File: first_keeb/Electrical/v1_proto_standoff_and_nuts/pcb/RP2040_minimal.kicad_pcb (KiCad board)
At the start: 4 copper layers, 67.1 x 66.8 mm, 81 parts, among them J1 Conn_01x04_Socket, J2 Conn_01x04_Socket, P1 USB-TYPE-C-016, Q1 SN74LV1T34DBV, SW1 SKRKAHE020, SW2 SKRKAHE020, SW3 BUTT1, SW4 BUTT3, SW5 BUTT2, SW6 MS-22C01-G010, SW7 SK-3296S-01-L3, SW8 MS-22C01-G010, U1 AMS1117-2.5, U2 ME6208A44M3G, U3 PRTR5V0U2X, U4 STM32F401RCTx, U5 MCP6001-OT, U6 MCP6001-OT, Y1 16MHz

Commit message: fixes lcsc number in bom
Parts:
- U7, U8, U9: value ~ -> SLSS49E
- Y1: value 16MHz -> 8MHz
- moved C13 0.05 mm to (83.7, 85.6)
- renumbered R5 to R4, R8 to R5, SW7 to SW1, SW6 to SW2, SW1 to SW3, SW8 to SW4, SW2 to SW5, SW3 to SW6, SW4 to SW7, SW5 to SW8, U5 to U4, U4 to U5
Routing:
- net GND: vias 230 -> 251

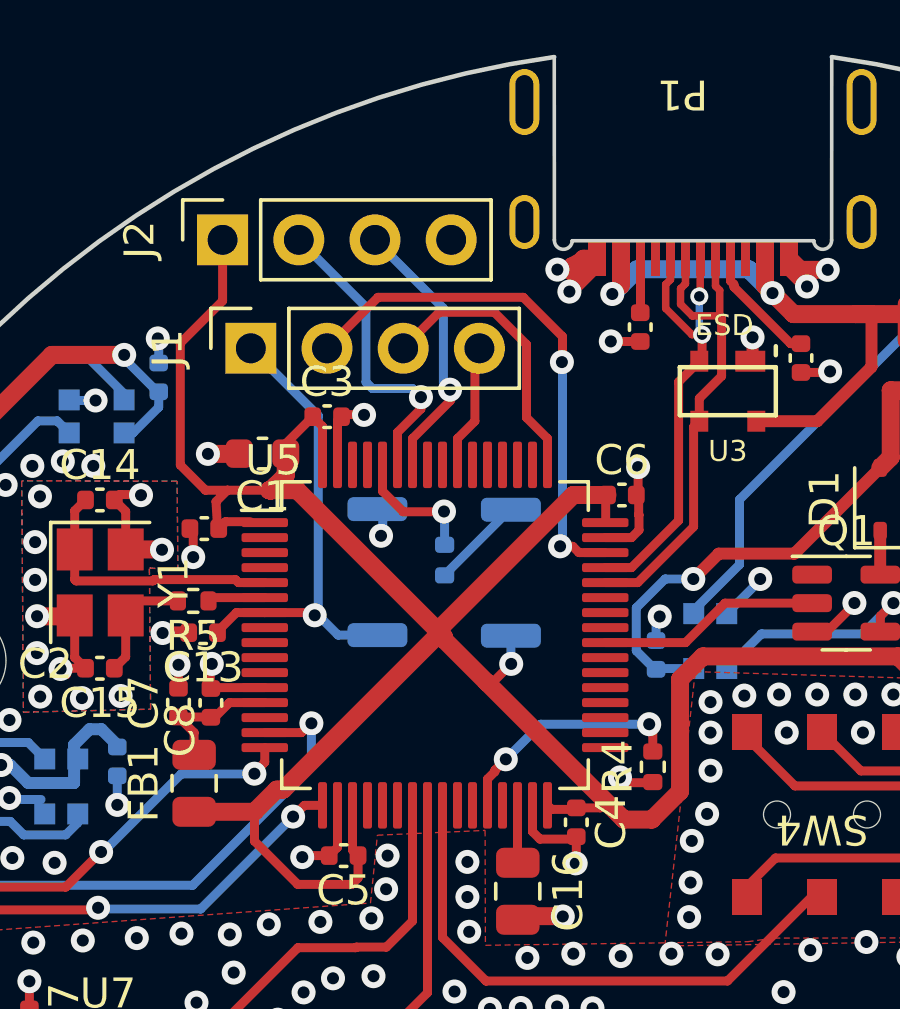
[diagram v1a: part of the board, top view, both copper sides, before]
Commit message: adds  basic part switch
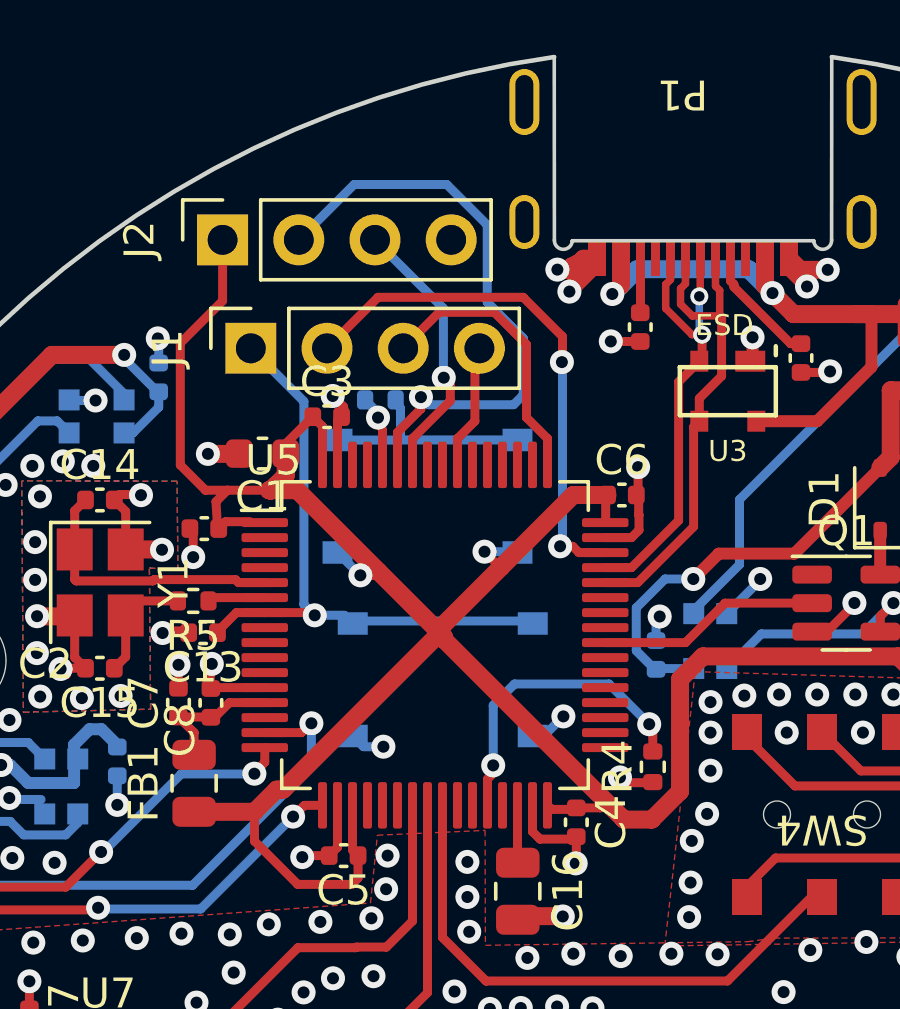
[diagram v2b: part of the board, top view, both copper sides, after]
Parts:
- SW3, SW5: value SKRKAHE020 -> TS-1187A-B-A-B; footprint Button_Switch_SMD:SW_Push_SPST_NO_Alps_SKRK -> Button_Switch_SMD:TS-1187A
- moved R3 5.75 mm to (89.6, 77.8), turned to 180 degrees
- moved SW5 4.20 mm to (91.7, 87.1), turned to 180 degrees
- moved SW3 3.77 mm to (91.2, 81.0), turned to 180 degrees
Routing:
- net USART1_RX: track 10.3 -> 20.0 mm
- net NRST: track 16.3 -> 20.7 mm
- net Net-(R3-Pad1): track 3.13 -> 7.03 mm
- net BOOT1: track 8.35 -> 10.8 mm
- net BOOT0: track 4.42 -> 2.37 mm
- net VDD: track 90.1 -> 91.6 mm, vias 1 -> 2
- net GND: track 123.2 -> 124.8 mm, vias 251 -> 252

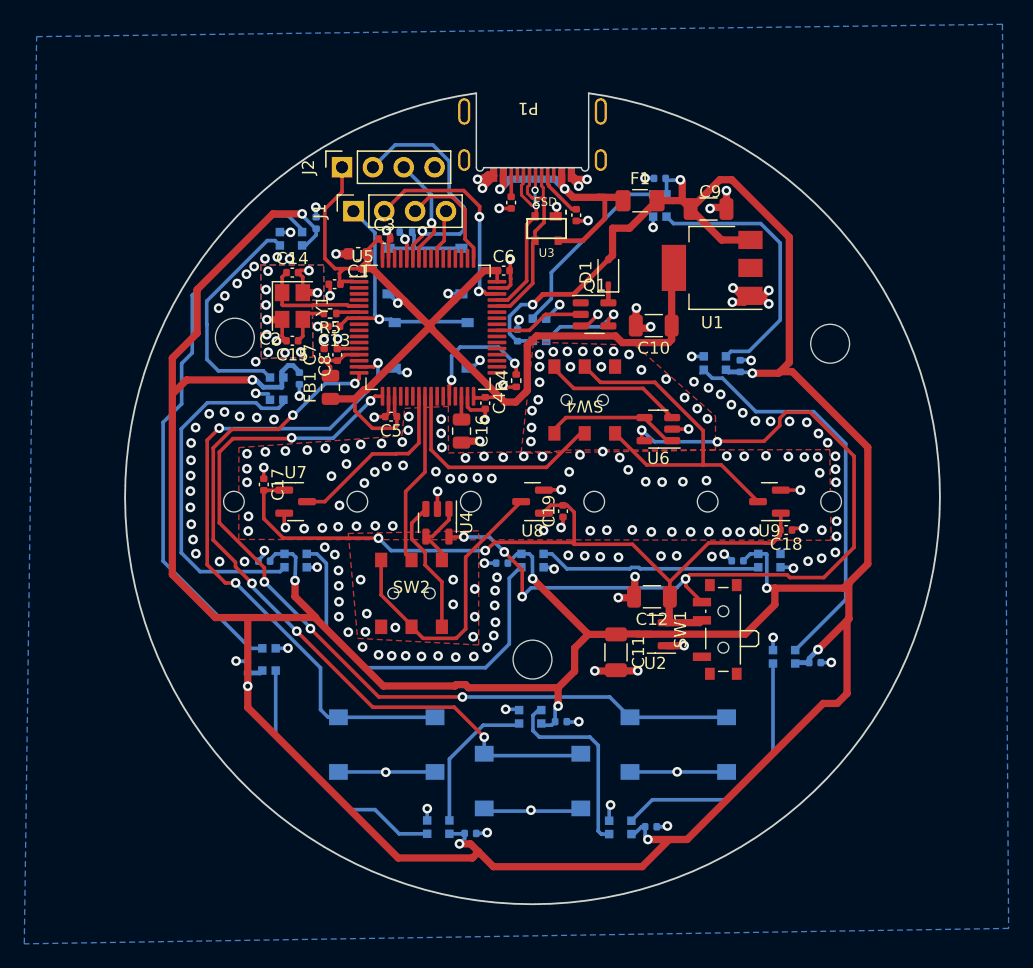
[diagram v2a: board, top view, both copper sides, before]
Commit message: creates plate for pcb
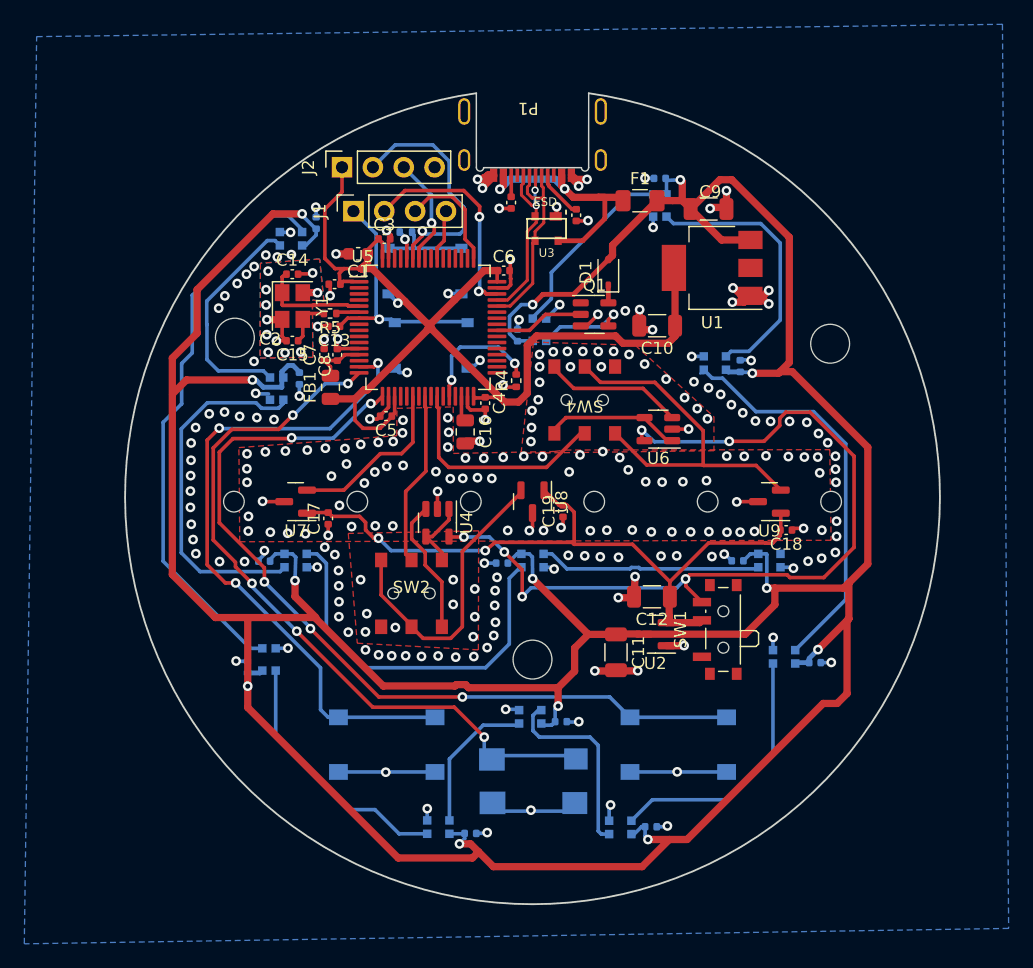
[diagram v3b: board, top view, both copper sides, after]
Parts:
- moved C17 5.99 mm to (83.2, 101.4), turned to 90 degrees
- moved C5 0.42 mm to (87.9, 93.0)
- moved C16 0.31 mm to (94.5, 94.3)
- moved C10 0.28 mm to (110.3, 85.5)
- moved C14 0.13 mm to (80.2, 81.3)
- turned U7 to 180 degrees
- turned U8 to -90 degrees
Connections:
- U5 pad 22: unconnected-(U5-PA6-Pad22) -> ADC_IN1
- U5 pad 23: ADC_IN1 -> unconnected-(U5-PA7-Pad23)
- U5 pad 25: ADC_IN3 -> unconnected-(U5-PC5-Pad25)
- U5 pad 26: unconnected-(U5-PB0-Pad26) -> ADC_IN3
- U7 pad 2: GND -> ADC_IN1
- U7 pad 3: ADC_IN1 -> GND
- U8 pad 2: GND -> S_ADC_IN2
- U8 pad 3: S_ADC_IN2 -> GND
- U9 pad 2: GND -> S_ADC_IN3
- U9 pad 3: S_ADC_IN3 -> GND
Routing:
- net +4V4: track 64.8 -> 57.9 mm
- net S_ADC_IN3: track 28.9 -> 30.4 mm
- net ADC_IN1: track 15.1 -> 13.6 mm
- net GND: track 124.8 -> 123.8 mm, vias 252 -> 254
- net +5V: track 324.7 -> 323.9 mm
- net S_ADC_IN2: track 24.1 -> 24.7 mm
- net BUTT1: track 61.8 -> 61.1 mm

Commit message: - no more tan caps - adds 1u before ferrite - ties ties other side of boot0 resistor to gnd
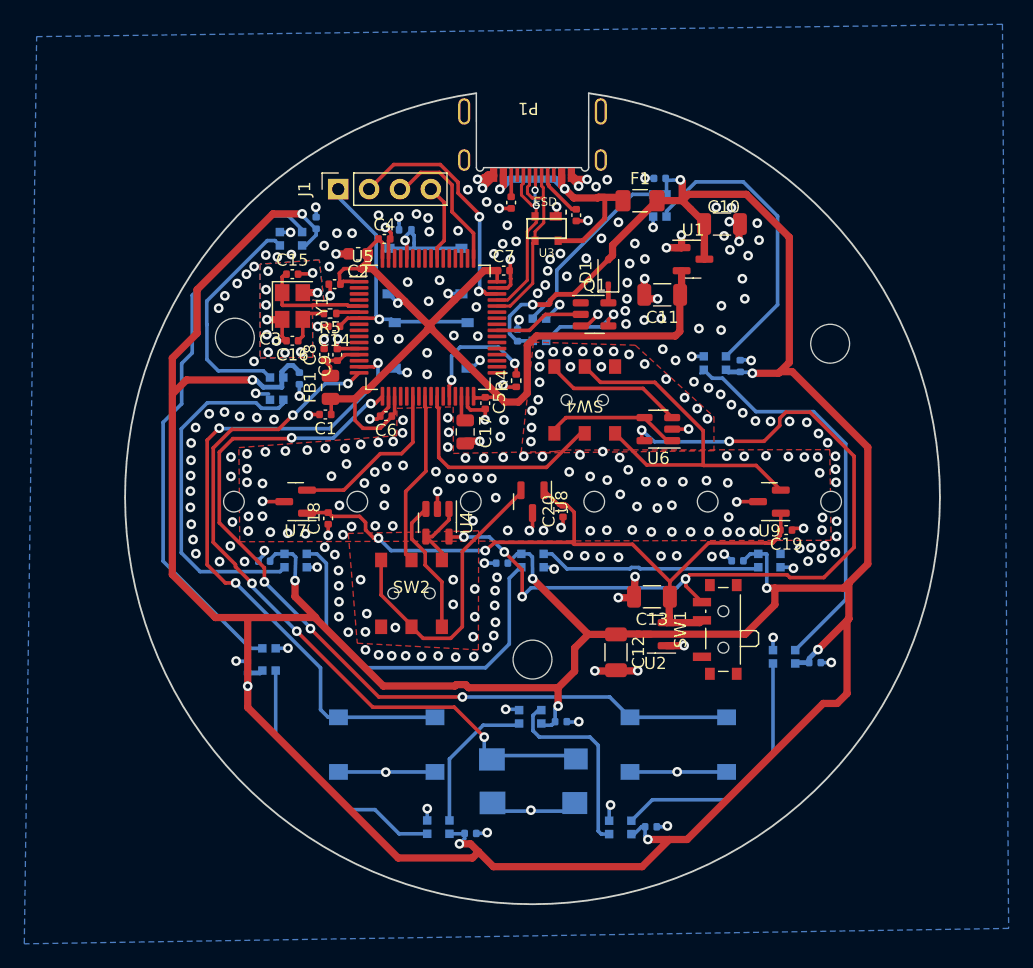
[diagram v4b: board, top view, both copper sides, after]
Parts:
- removed J2: Conn_01x04_Socket, Connector_PinSocket_2.54mm:PinSocket_1x04_P2.54mm_Vertical
- added C1: 1u, Capacitor_SMD:C_0402_1005Metric, F.Cu at (83.0, 92.8)
- C10: renamed from C9; value 10u -> 22u
- C11: renamed from C10; value 10u -> 22u
- C12: renamed from C11; value 10u -> 22u
- C13: renamed from C12; value 10u -> 22u
- C17: renamed from C16; value 4.7u -> 4u7
- U1: value AMS1117-2.5 -> ME6206A25XG; footprint Package_TO_SOT_SMD:SOT-223-3_TabPin2 -> Package_TO_SOT_SMD:SOT-23
- moved C11 2.58 mm to (110.7, 83.0)
- moved J1 2.20 mm to (84.0, 74.3)
- moved U1 1.73 mm to (113.2, 80.0), turned to 0 degrees
- moved C10 1.66 mm to (115.6, 77.2)
- moved R3 0.19 mm to (89.5, 77.6)
- renumbered C13 to C14, C14 to C15, C15 to C16, C17 to C18, C18 to C19, C1 to C2, C19 to C20, C20 to C21, C21 to C22, C22 to C23, C23 to C24, C24 to C25, C25 to C26, C26 to C27, C27 to C28, C28 to C29, C2 to C3, C29 to C30, C30 to C31, C31 to C32, C32 to C33, C3 to C4, C4 to C5, C5 to C6, C6 to C7, C7 to C8, C8 to C9
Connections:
- R3 pad 1: Net-(R3-Pad1) -> BOOT0
- R3 pad 2: BOOT0 -> GND
- SW3 pad 1: Net-(R3-Pad1) -> BOOT0
- U5 pad 58: USART1_TX -> unconnected-(U5-PB6-Pad58)
- U5 pad 59: USART1_RX -> unconnected-(U5-PB7-Pad59)
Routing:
- net USART1_RX: track 20.0 -> 0.00 mm, vias 1 -> 0
- net USART1_TX: track 9.06 -> 0.00 mm, vias 1 -> 0
- net VDD: track 91.6 -> 83.1 mm
- net BOOT0: track 2.37 -> 9.64 mm
- net Net-(R3-Pad1): track 7.03 -> 0.00 mm
- net GND: track 123.8 -> 120.7 mm, vias 254 -> 337
- net Net-(D3-DOUT): track 22.3 -> 25.1 mm
- net SWCLK: track 9.35 -> 12.1 mm
- net SWDIO: track 17.6 -> 20.0 mm
- net NRST: track 20.7 -> 23.1 mm
- net SWO: track 4.19 -> 6.40 mm
- net +5V: track 323.9 -> 323.3 mm
